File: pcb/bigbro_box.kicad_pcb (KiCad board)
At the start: 2 copper layers, 100 x 58 mm, 50 parts, among them J1 Current Sense, J2 Display, J3 Mains, J4 Debug, J5 RFID, J6 Relay, J7 Ext, K1 G5LE-1, Q1 MMBT3904, Q2 MMBT3904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

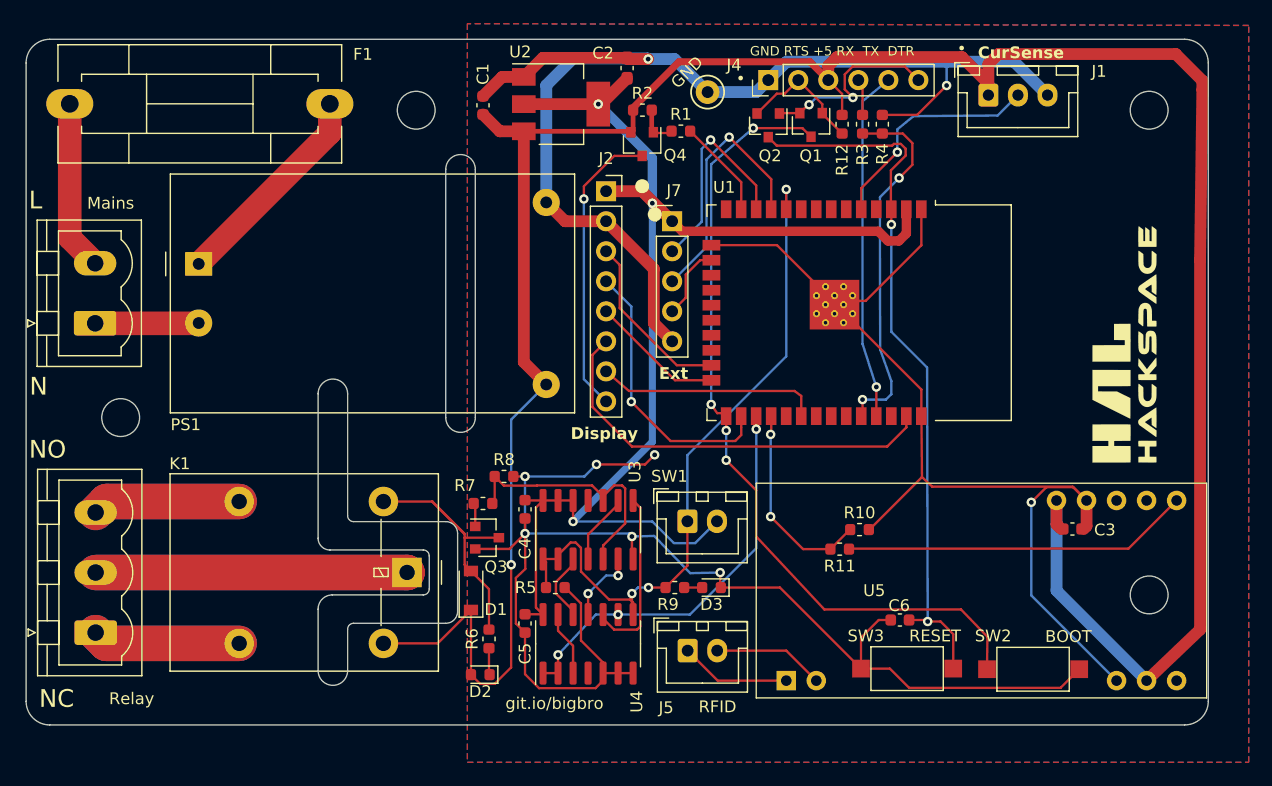
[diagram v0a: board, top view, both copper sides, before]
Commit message: Use a smaller fuse.
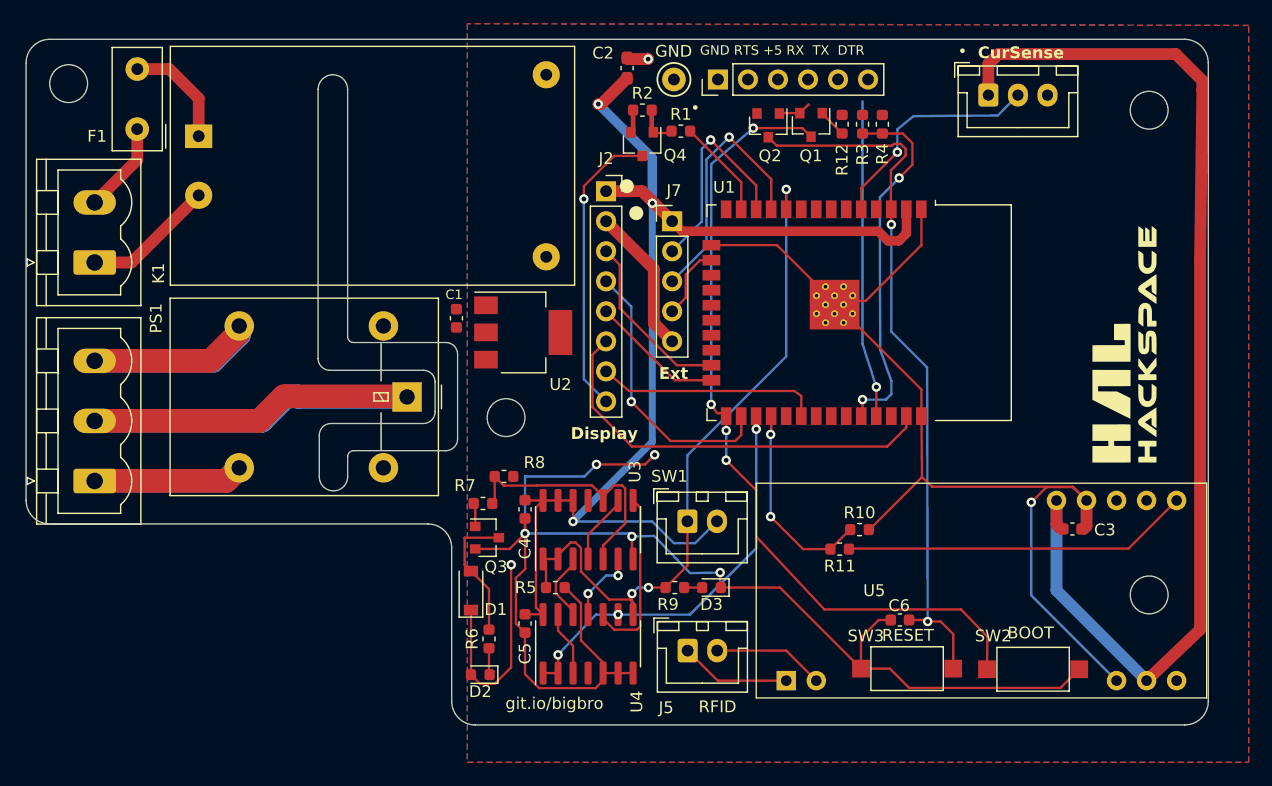
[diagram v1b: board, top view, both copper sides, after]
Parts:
- F1: footprint modules:Fuseholder5x20_horiz_SemiClosed_Casing10x25mm -> Fuse:Fuse_Littelfuse_395Series
- moved H1 32.6 mm to (106.6, 89.0)
- moved H2 29.5 mm to (69.6, 60.8)
- moved U2 19.6 mm to (108.0, 81.8)
- moved C1 18.2 mm to (102.4, 80.6)
- moved K1 14.8 mm to (98.2, 87.2)
- moved J6 12.8 mm to (71.8, 94.4)
- moved PS1 10.8 mm to (80.6, 65.2)
- moved F1 6.09 mm to (75.4, 64.6), turned to 90 degrees
- moved J3 5.15 mm to (71.8, 75.9)
- moved J4 4.26 mm to (124.5, 60.4)
- moved TP11 3.04 mm to (120.8, 60.4)
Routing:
- net +5V: track 215.7 -> 117.3 mm
- net GND: track 304.9 -> 219.6 mm, vias 9 -> 7
- net /~{DTR}: track 16.0 -> 2.81 mm, vias 2 -> 0
- net Net-(D1-A): track 23.7 -> 11.5 mm
- net Net-(PS1-AC/L): track 18.1 -> 9.42 mm
- net ~{RTS}: track 10.7 -> 2.42 mm
- net Net-(J3-Pin_2): track 14.4 -> 7.69 mm
- net +3V3: track 112.3 -> 106.0 mm
- net Net-(J4-Pin_4): track 3.09 -> 0.00 mm
- net /MCU_TX0: track 29.4 -> 26.6 mm
- net /NO: track 25.1 -> 27.6 mm
- net Net-(J3-Pin_1): track 8.77 -> 11.2 mm
- net /COM: track 52.7 -> 54.6 mm
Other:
- outline, holes or cut-outs redrawn
- board text added: "C"
- board text added: "TODO: - dobbeltbaner ved relæ - ground plane keepout - current sense diode++"

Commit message: Add extra transistor.
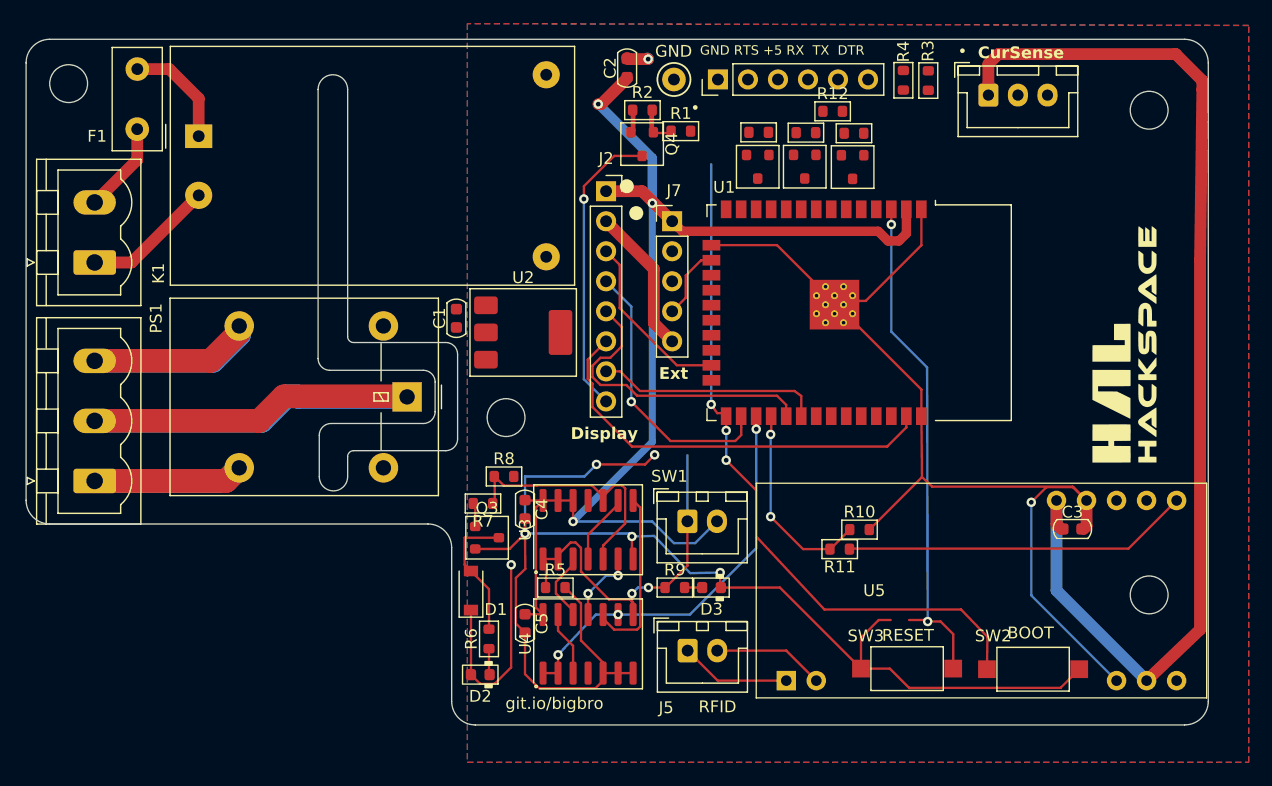
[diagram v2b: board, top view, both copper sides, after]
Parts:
- removed C6: 100n, Capacitor_SMD:C_0603_1608Metric
- added Q5: MMBT3904, PCM_Package_TO_SOT_SMD_AKL:SOT-23, F.Cu at (127.9, 67.8)
- added R13: 1k, PCM_Resistor_SMD_AKL:R_0603_1608Metric, F.Cu at (132.0, 64.9)
- added R14: 1k, PCM_Resistor_SMD_AKL:R_0603_1608Metric, F.Cu at (136.0, 64.9)
- added R15: 1k, PCM_Resistor_SMD_AKL:R_0603_1608Metric, F.Cu at (128.0, 64.9)
- C1, C3, C4, C5: footprint Capacitor_SMD:C_0603_1608Metric -> PCM_Capacitor_SMD_AKL:C_0603_1608Metric
- C2: footprint Capacitor_SMD:C_0603_1608Metric_Pad1.08x0.95mm_HandSolder -> PCM_Capacitor_SMD_AKL:C_0603_1608Metric
- D2, D3: footprint LED_SMD:LED_0603_1608Metric -> PCM_LED_SMD_AKL:LED_0603_1608Metric
- Q1, Q2, Q3, Q4: footprint Package_TO_SOT_SMD:SOT-23 -> PCM_Package_TO_SOT_SMD_AKL:SOT-23
- R1, R10, R11, R12, R2, R3, R4, R5, R6, R7, R8, R9: footprint Resistor_SMD:R_0603_1608Metric -> PCM_Resistor_SMD_AKL:R_0603_1608Metric
- U2: footprint Package_TO_SOT_SMD:SOT-223-3_TabPin2 -> PCM_Package_TO_SOT_SMD_AKL:SOT-223-3_TabPin2
- U3, U4: footprint Package_SO:SOIC-14_3.9x8.7mm_P1.27mm -> PCM_Package_SO_AKL:SOIC-14_3.9x8.7mm_P1.27mm
- moved R4 5.36 mm to (142.3, 60.5)
- moved R3 5.08 mm to (140.2, 60.5)
- moved Q1 5.01 mm to (135.9, 67.8)
- moved Q2 4.67 mm to (131.9, 67.8)
- moved R12 1.35 mm to (134.2, 63.1), turned to 0 degrees
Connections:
- net /MCU_RX0 renamed RX
- net /MCU_TX0 renamed TX
- net /~{BOOT} renamed ~{BOOT}
- net /~{RESET} renamed ~{RESET}
- net Display_backlight renamed Backlight
- J4 pad 6: /~{DTR} -> ~{DTR}
- Q1 pad 1: ~{RTS} -> Net-(Q1-B)
- Q1 pad 2: /~{DTR} -> ~{DTR}
- Q2 pad 1: /~{DTR} -> Net-(Q2-B)
- U1 pad 24: Display_A0 -> IO2
- U1 pad 29: unconnected-(U1-IO5-Pad29) -> Display_A0
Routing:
- net RX: track 30.9 -> 0.14 mm, vias 2 -> 0
- net /card_switch: track 59.9 -> 32.0 mm, vias 3 -> 2
- net TX: track 26.6 -> 0.00 mm, vias 1 -> 0
- net Ext2: track 22.0 -> 0.00 mm, vias 1 -> 0
- net /CurrentSense: track 19.6 -> 0.00 mm, vias 1 -> 0
- net Ext3: track 18.5 -> 0.00 mm, vias 1 -> 0
- net ~{RESET}: track 61.1 -> 43.1 mm
- net Display_A0: track 11.6 -> 25.9 mm
- net ~{BOOT}: track 69.3 -> 59.4 mm, vias 4 -> 3
- net Backlight: track 8.65 -> 0.00 mm
- net /~{DTR}: track 2.81 -> 0.00 mm
- net ~{RTS}: track 2.42 -> 0.00 mm

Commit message: Route.
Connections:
- net /card_switch renamed SW
- net /relay renamed RELAY
- net /relay_gpio renamed RELAY_EN
- net /~{card_switch} renamed Net-(U4-Pad13)
- net /~{relay_gpio} renamed Net-(U3-Pad3)
- J1 pad 2: /CurrentSense -> SENSE
- U1 pad 5: /CurrentSense -> unconnected-(U1-SENSOR_VN-Pad5)
- U1 pad 6: unconnected-(U1-IO34-Pad6) -> SENSE
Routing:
- net +5V: track 117.3 -> 183.4 mm
- net GND: track 219.6 -> 263.2 mm
- net ~{RTS}: track 0.00 -> 26.2 mm
- net SW: track 32.0 -> 56.4 mm, vias 2 -> 3
- net +3V3: track 106.0 -> 127.5 mm, vias 3 -> 5
- net IO2: track 0.00 -> 20.6 mm, vias 0 -> 2
- net ~{DTR}: track 0.00 -> 19.5 mm
- net SENSE: track 0.00 -> 19.1 mm, vias 0 -> 1
- net Ext2: track 0.00 -> 10.9 mm, vias 0 -> 1
- net Net-(J4-Pin_4): track 0.00 -> 8.71 mm
- net Ext3: track 0.00 -> 8.58 mm, vias 0 -> 1
- net Backlight: track 0.00 -> 8.38 mm
- net ~{RESET}: track 43.1 -> 50.6 mm
- net ~{BOOT}: track 59.4 -> 63.1 mm, vias 3 -> 4
- net RX: track 0.14 -> 2.26 mm
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
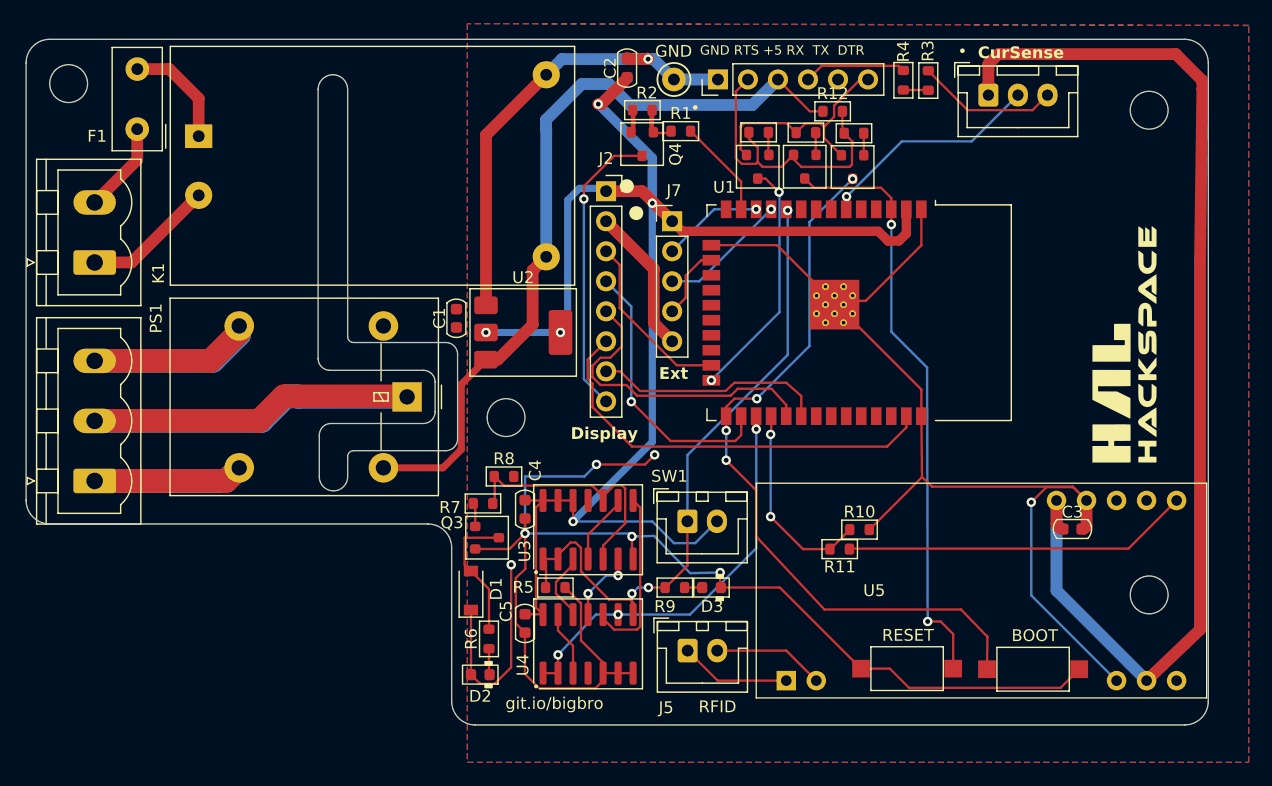
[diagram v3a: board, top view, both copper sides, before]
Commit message: Finish routing.
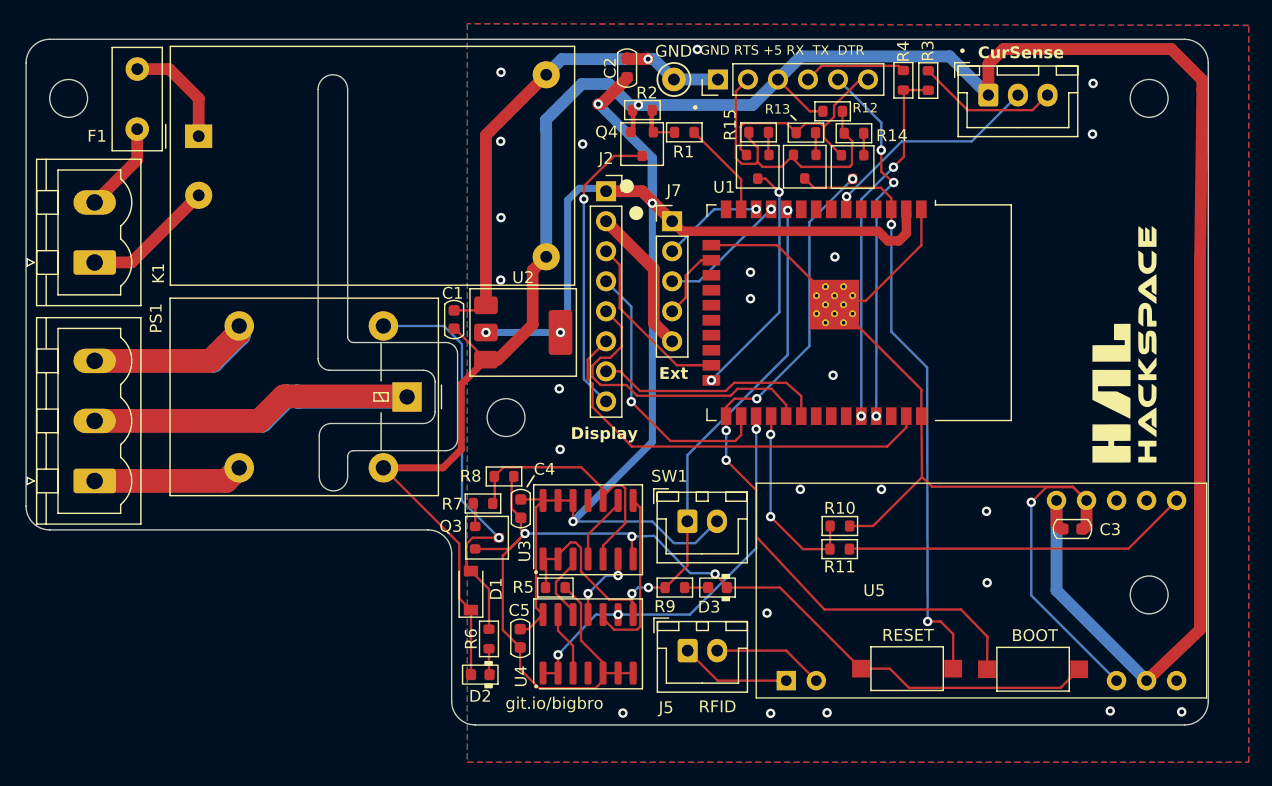
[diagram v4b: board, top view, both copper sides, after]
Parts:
- moved R10 1.69 mm to (134.8, 98.2)
- moved C5 1.32 mm to (107.8, 107.7)
- moved H2 1.25 mm to (69.6, 62.0)
- moved H3 1.00 mm to (161.0, 62.0)
- moved D3 0.51 mm to (124.5, 103.4)
- moved C4 0.36 mm to (107.8, 96.7)
- moved R1 0.31 mm to (121.7, 64.9)
- moved C1 0.22 mm to (102.2, 80.7)
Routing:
- net TX: track 0.00 -> 31.1 mm, vias 0 -> 3
- net RX: track 2.26 -> 31.4 mm, vias 0 -> 2
- net +5V: track 183.4 -> 210.3 mm
- net Net-(D1-A): track 11.5 -> 36.0 mm, vias 0 -> 1
- net GND: track 263.2 -> 255.4 mm, vias 7 -> 29
- net RELAY: track 21.7 -> 23.1 mm
- net +3V3: track 127.5 -> 128.9 mm
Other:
- outline, holes or cut-outs redrawn
- board text removed: "TODO: - dobbeltbaner ved relæ - ground plane keepout - current sense diode++"

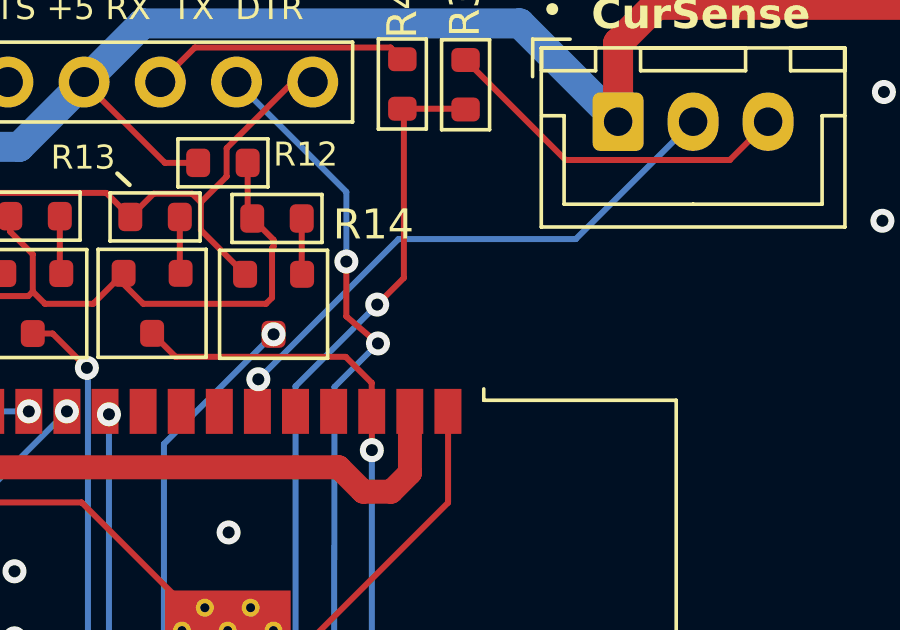
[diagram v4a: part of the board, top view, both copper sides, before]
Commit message: Start adding JLCPCB part numbers.
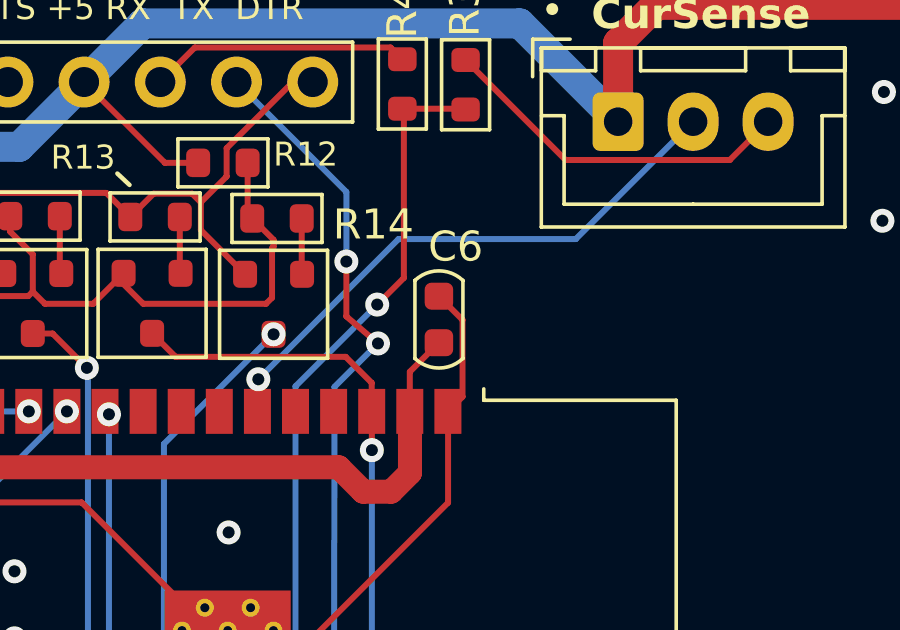
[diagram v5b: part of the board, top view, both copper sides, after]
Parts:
- added C6: 100n, PCM_Capacitor_SMD_AKL:C_0603_1608Metric, F.Cu at (141.4, 68.3)
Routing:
- net GND: track 255.4 -> 259.8 mm
- net +3V3: track 128.9 -> 131.6 mm
